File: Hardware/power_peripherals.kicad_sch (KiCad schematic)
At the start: 46 parts, among them J10 microSD_Friction, J11 Qwiic_RA, J5 Conn_01x10, J6 Conn_01x10, J7 Conn_01x10, J8 Conn_01x10, J9 JST_2mm_LiPo, Q1 DMG2305UX, SW2 SMD_4.6x2.8mm_h2.5mm, SW3 SMD_4.6x2.8mm_h2.5mm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

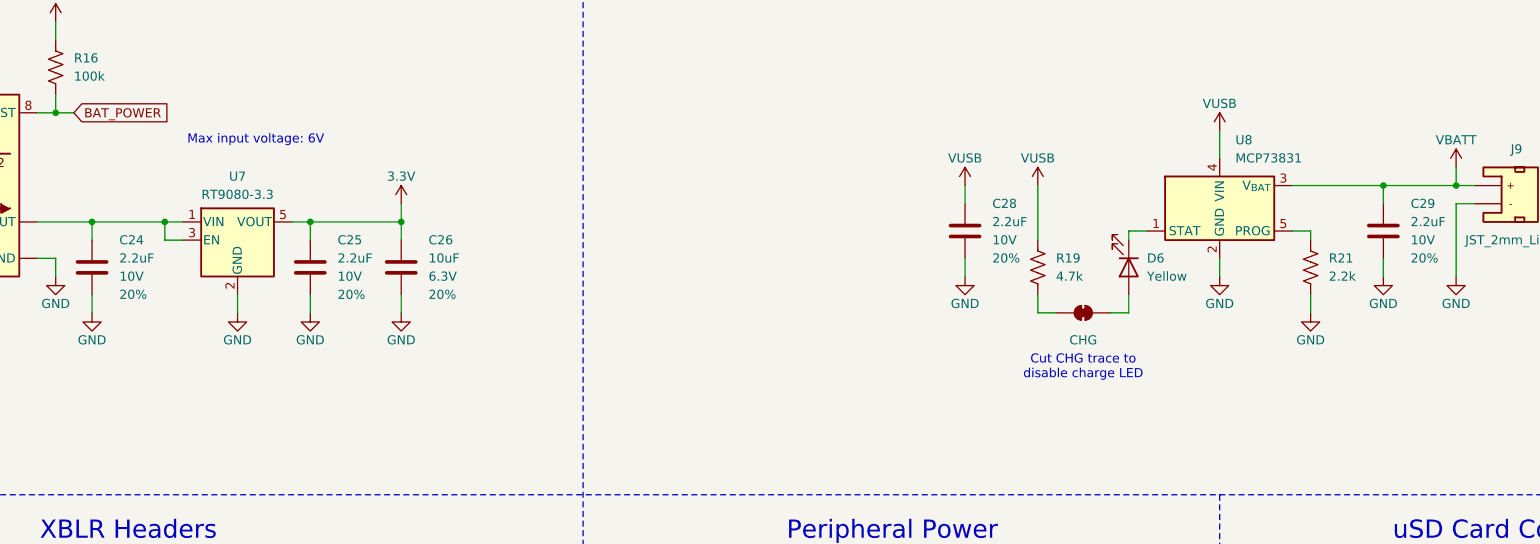
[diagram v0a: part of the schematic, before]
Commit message: Design review updates
Move text for D1 and D3 to not overlap wire
Add regulator max output current
Add battery charge current
Add (R) to LoRaWAN silkscreen
Name copper zones
Nudge mesaure text on let side to not overlap lines
Add measures from center to edge of board
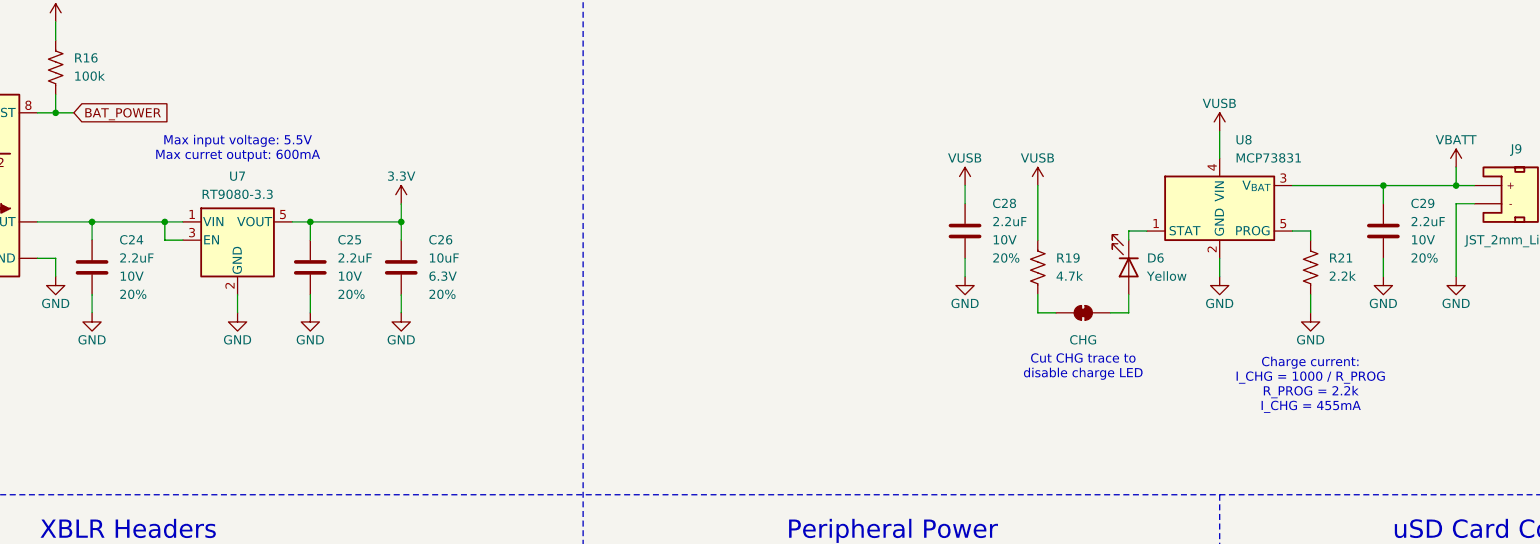
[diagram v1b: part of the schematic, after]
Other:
- note added: "Charge current: I_CHG = 1000 / R_PROG R_PROG = 2.2k I_CHG = 455mA"
- note added: "Max input voltage: 5.5V Max curret output: 600mA"
- note removed: "Max input voltage: 6V"
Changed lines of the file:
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@@
+		)
+	)
+	(text "Charge current:\nI_CHG = 1000 / R_PROG\nR_PROG = 2.2k\nI_CHG = 455mA"
+		(exclude_from_sim no)
+		(at 241.3 86.36 0)
+		(effects
+			(font
+				(size 1.27 1.27)
+			)
 		)
 	)
@@
 		)
 	)
-	(text "Max input voltage: 6V"
+	(text "Max input voltage: 5.5V\nMax curret output: 600mA"
 		(exclude_from_sim no)
-		(at 93.98 52.07 0)
+		(at 91.44 53.34 0)
 		(effects
 			(font
